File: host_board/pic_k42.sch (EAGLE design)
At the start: 57 parts, among them IC1 PIC18F57K42-E_PT, IC2 REF3440IDBVR, IC3 MAX232, IC4 ILAMP, K1 G6K-2P, Q1 ASF1, X1 RX-2, X2 TX-2, X3 RESETJMP, X4 MINI-USB-UX60A-MB-5ST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

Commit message: mbmc version
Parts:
- added R12: 220, rcl:R-US_R1206
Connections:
- new net N$70: C1.1, R12.1, R2.1, S4.4, X3-2.S
- net N$1: now also R12.2; no longer C1.1, R2.1, S4.4, X3-2.S
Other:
- moved on the sheet: C1, R2
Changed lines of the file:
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@@
 <?xml version="1.0" encoding="utf-8"?>
 <!DOCTYPE eagle SYSTEM "eagle.dtd">
-<eagle version="9.5.0">
+<eagle version="9.5.1">
 <drawing>
 <settings>
@@
 <part name="TP2" library="testpad" library_urn="urn:adsk.eagle:library:385" deviceset="TP" device="B1,27" package3d_urn="urn:adsk.eagle:package:27944/2"/>
 <part name="VDD10" library="supply1" library_urn="urn:adsk.eagle:library:371" deviceset="VDD" device=""/>
+<part name="R12" library="rcl" library_urn="urn:adsk.eagle:library:334" deviceset="R-US_" device="R1206" package3d_urn="urn:adsk.eagle:package:23540/2" value="220"/>
 </parts>
 <sheets>
@@
 <attribute name="VALUE" x="61.722" y="1.27" size="1.778" layer="96" rot="R90"/>
 </instance>
-<instance part="R2" gate="G$1" x="53.34" y="0" smashed="yes" rot="R180">
-<attribute name="NAME" x="57.15" y="-1.4986" size="1.778" layer="95" rot="R180"/>
-<attribute name="VALUE" x="57.15" y="3.302" size="1.778" layer="96" rot="R180"/>
-</instance>
-<instance part="C1" gate="G$1" x="58.42" y="-2.54" smashed="yes">
-<attribute name="NAME" x="59.436" y="-1.905" size="1.778" layer="95"/>
-<attribute name="VALUE" x="59.436" y="-6.731" size="1.778" layer="96"/>
-</instance>
-<instance part="VDD1" gate="G$1" x="45.72" y="0" smashed="yes" rot="R90">
-<attribute name="VALUE" x="48.26" y="-2.54" size="1.778" layer="96" rot="R180"/>
-</instance>
-<instance part="VSS1" gate="G$1" x="58.42" y="-10.16" smashed="yes">
-<attribute name="VALUE" x="55.88" y="-15.24" size="1.778" layer="96" rot="R90"/>
+<instance part="R2" gate="G$1" x="53.34" y="-10.16" smashed="yes" rot="R180">
+<attribute name="NAME" x="57.15" y="-11.6586" size="1.778" layer="95" rot="R180"/>
+<attribute name="VALUE" x="57.15" y="-6.858" size="1.778" layer="96" rot="R180"/>
+</instance>
+<instance part="C1" gate="G$1" x="58.42" y="-12.7" smashed="yes">
+<attribute name="NAME" x="59.436" y="-12.065" size="1.778" layer="95"/>
+<attribute name="VALUE" x="59.436" y="-16.891" size="1.778" layer="96"/>
+</instance>
+<instance part="VDD1" gate="G$1" x="48.26" y="2.54" smashed="yes">
+<attribute name="VALUE" x="45.72" y="0" size="1.778" layer="96" rot="R90"/>
+</instance>
+<instance part="VSS1" gate="G$1" x="50.8" y="-20.32" smashed="yes">
+<attribute name="VALUE" x="48.26" y="-25.4" size="1.778" layer="96" rot="R90"/>
 </instance>
 <instance part="VDD2" gate="G$1" x="58.42" y="-22.86" smashed="yes" rot="R90">
@@
 <instance part="VDD10" gate="G$1" x="-106.68" y="-48.26" smashed="yes" rot="R180">
 <attribute name="VALUE" x="-104.14" y="-45.72" size="1.778" layer="96" rot="R270"/>
+</instance>
+<instance part="R12" gate="G$1" x="58.42" y="-5.08" smashed="yes" rot="R90">
+<attribute name="NAME" x="56.9214" y="-8.89" size="1.778" layer="95" rot="R90"/>
+<attribute name="VALUE" x="61.722" y="-8.89" size="1.778" layer="96" rot="R90"/>
 </instance>
 </instances>
@@
 </busses>
 <nets>
-<net name="N$1" class="0">
-<segment>
-<pinref part="R1" gate="G$1" pin="1"/>
-<pinref part="R2" gate="G$1" pin="1"/>
-<pinref part="C1" gate="G$1" pin="1"/>
-<junction x="58.42" y="0"/>
-<pinref part="SV1" gate="1" pin="1"/>
-<wire x1="63.5" y1="-50.8" x2="63.5" y2="-17.78" width="0.1524" layer="91"/>
-<wire x1="63.5" y1="-17.78" x2="63.5" y2="0" width="0.1524" layer="91"/>
-<wire x1="63.5" y1="0" x2="58.42" y2="0" width="0.1524" layer="91"/>
-<junction x="63.5" y="-50.8"/>
-<wire x1="63.5" y1="0" x2="73.66" y2="0" width="0.1524" layer="91"/>
-<pinref part="X3" gate="-2" pin="S"/>
-<wire x1="73.66" y1="0" x2="73.66" y2="7.62" width="0.1524" layer="91"/>
-<junction x="63.5" y="0"/>
-<junction x="73.66" y="7.62"/>
-<wire x1="63.5" y1="-17.78" x2="139.7" y2="-17.78" width="0.1524" layer="91"/>
-<junction x="63.5" y="-17.78"/>
-<wire x1="139.7" y1="-17.78" x2="139.7" y2="-35.56" width="0.1524" layer="91"/>
-<wire x1="139.7" y1="-35.56" x2="167.64" y2="-35.56" width="0.1524" layer="91"/>
-<pinref part="S4" gate="G$1" pin="4"/>
-<wire x1="167.64" y1="-35.56" x2="167.64" y2="-43.18" width="0.1524" layer="91"/>
-<junction x="167.64" y="-43.18"/>
-</segment>
-</net>
 <net name="N$2" class="0">
 <segment>
@@
 <wire x1="58.42" y1="17.78" x2="58.42" y2="10.16" width="0.1524" layer="91"/>
 <junction x="58.42" y="17.78"/>
+<junction x="58.42" y="10.16"/>
 </segment>
 </net>
@@
 <pinref part="R2" gate="G$1" pin="2"/>
 <pinref part="VDD1" gate="G$1" pin="VDD"/>
-<junction x="48.26" y="0"/>
+<wire x1="48.26" y1="-10.16" x2="48.26" y2="0" width="0.1524" layer="91"/>
+<junction x="48.26" y="-10.16"/>
 </segment>
 <segment>
@@
 <pinref part="VDD2" gate="G$1" pin="VDD"/>
 <junction x="60.96" y="-50.8"/>
+<junction x="60.96" y="-22.86"/>
 </segment>
 <segment>
@@
 <pinref part="VSS2" gate="G$1" pin="VSS"/>
 <junction x="58.42" y="-50.8"/>
+<junction x="58.42" y="-30.48"/>
 </segment>
 <segment>
@@
 <pinref part="C1" gate="G$1" pin="2"/>
 <pinref part="VSS1" gate="G$1" pin="VSS"/>
-<junction x="58.42" y="-7.62"/>
+<wire x1="50.8" y1="-17.78" x2="58.42" y2="-17.78" width="0.1524" layer="91"/>
+<junction x="58.42" y="-17.78"/>
+<junction x="50.8" y="-17.78"/>
 </segment>
 <segment>
@@
 </segment>
 </net>
+<net name="N$70" class="0">
+<segment>
+<pinref part="C1" gate="G$1" pin="1"/>
+<pinref part="R2" gate="G$1" pin="1"/>
+<pinref part="R12" gate="G$1" pin="1"/>
+<pinref part="R12" gate="G$1" pin="1"/>
+<junction x="58.42" y="-10.16"/>
+<junction x="58.42" y="-10.16"/>
+<wire x1="58.42" y1="-10.16" x2="66.04" y2="-10.16" width="0.1524" layer="91"/>
+<wire x1="66.04" y1="-10.16" x2="66.04" y2="-25.4" width="0.1524" layer="91"/>
+<wire x1="66.04" y1="-25.4" x2="76.2" y2="-25.4" width="0.1524" layer="91"/>
+<pinref part="X3" gate="-2" pin="S"/>
+<junction x="73.66" y="7.62"/>
+<wire x1="73.66" y1="-2.54" x2="73.66" y2="7.62" width="0.1524" layer="91"/>
+<wire x1="73.66" y1="-2.54" x2="76.2" y2="-2.54" width="0.1524" layer="91"/>
+<wire x1="76.2" y1="-17.78" x2="139.7" y2="-17.78" width="0.1524" layer="91"/>
+<wire x1="139.7" y1="-17.78" x2="139.7" y2="-35.56" width="0.1524" layer="91"/>
+<wire x1="139.7" y1="-35.56" x2="167.64" y2="-35.56" width="0.1524" layer="91"/>
+<pinref part="S4" gate="G$1" pin="4"/>
+<wire x1="167.64" y1="-35.56" x2="167.64" y2="-43.18" width="0.1524" layer="91"/>
+<junction x="167.64" y="-43.18"/>
+<wire x1="76.2" y1="-2.54" x2="76.2" y2="-17.78" width="0.1524" layer="91"/>
+<wire x1="76.2" y1="-25.4" x2="76.2" y2="-17.78" width="0.1524" layer="91"/>
+<junction x="76.2" y="-17.78"/>
+</segment>
+</net>
+<net name="N$1" class="0">
+<segment>
+<pinref part="R1" gate="G$1" pin="1"/>
+<pinref part="R12" gate="G$1" pin="2"/>
+<junction x="58.42" y="0"/>
+<wire x1="58.42" y1="0" x2="63.5" y2="0" width="0.1524" layer="91"/>
+<pinref part="SV1" gate="1" pin="1"/>
+<wire x1="63.5" y1="-50.8" x2="63.5" y2="0" width="0.1524" layer="91"/>
+<junction x="63.5" y="-50.8"/>
+</segment>
+</net>

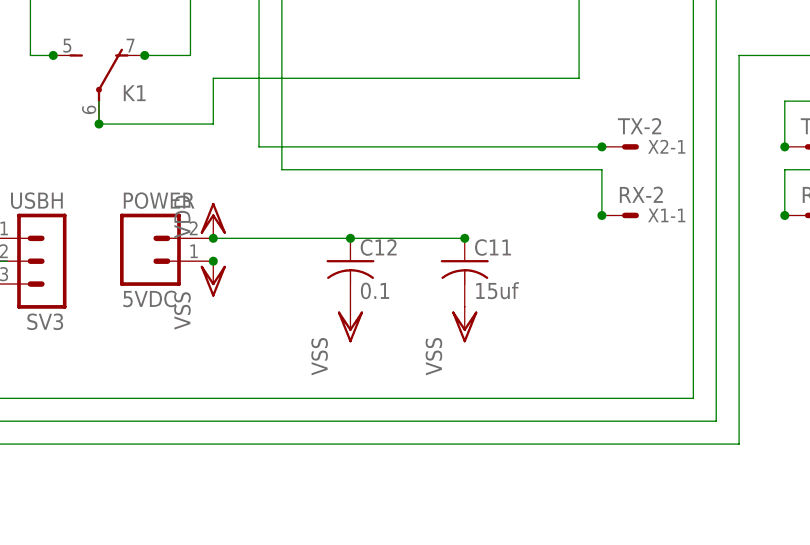
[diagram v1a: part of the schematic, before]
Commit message: up host board to v1.7
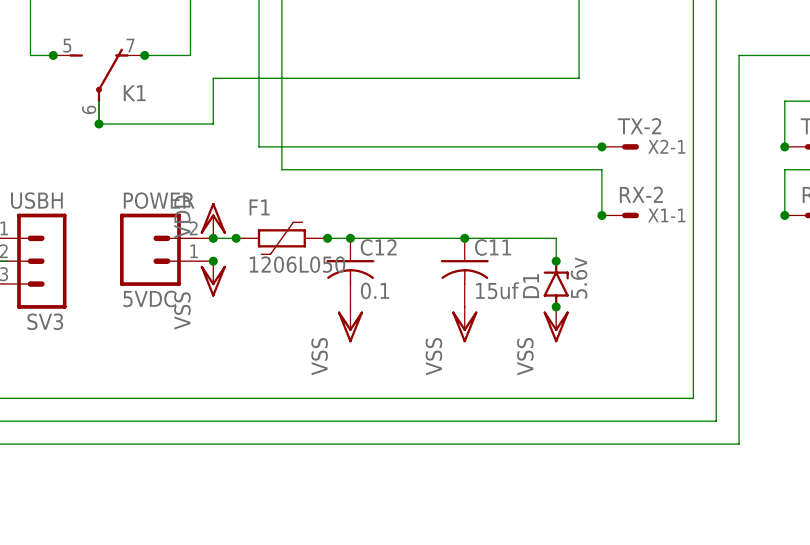
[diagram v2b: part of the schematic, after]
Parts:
- added D1: 5.6v, diode:ZENER-DIODEDO34-7
- added F1: 1206L050, polyfuse-smd_10:1206L050
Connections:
- new net N$71: C11.1, C12.1, D1.C, F1.1
- net VDD: now also F1.2; no longer C11.1, C12.1
- net VSS: now also D1.A
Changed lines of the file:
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@@
 <layer number="97" name="Info" color="7" fill="1" visible="yes" active="yes"/>
 <layer number="98" name="Guide" color="6" fill="1" visible="yes" active="yes"/>
+<layer number="99" name="SpiceOrder" color="5" fill="1" visible="yes" active="yes"/>
 </layers>
 <schematic xreflabel="%F%N/%S.%C%R" xrefpart="/%S.%C%R">
@@
 <classes>
 <class number="0" name="default" width="0" drill="0">
+</class>
+<class number="1" name="i-line" width="0.3" drill="0">
 </class>
 </classes>
@@
 <part name="VDD10" library="supply1" library_urn="urn:adsk.eagle:library:371" deviceset="VDD" device=""/>
 <part name="R12" library="rcl" library_urn="urn:adsk.eagle:library:334" deviceset="R-US_" device="R1206" package3d_urn="urn:adsk.eagle:package:23540/2" value="220"/>
+<part name="VSS16" library="supply1" library_urn="urn:adsk.eagle:library:371" deviceset="VSS" device=""/>
+<part name="F1" library="polyfuse-smd_10" deviceset="?" device="1206L" technology="050"/>
+<part name="D1" library="diode" library_urn="urn:adsk.eagle:library:210" deviceset="ZENER-DIODE" device="DO34-7" package3d_urn="urn:adsk.eagle:package:43364/1" value="5.6v"/>
 </parts>
 <sheets>
@@
 <attribute name="VALUE" x="61.722" y="-8.89" size="1.778" layer="96" rot="R90"/>
 </instance>
+<instance part="VSS16" gate="G$1" x="-7.62" y="-50.8" smashed="yes">
+<attribute name="VALUE" x="-10.16" y="-55.88" size="1.778" layer="96" rot="R90"/>
+</instance>
+<instance part="F1" gate="G$1" x="-38.1" y="-40.64" smashed="yes">
+<attribute name="NAME" x="-41.91" y="-38.1" size="1.778" layer="95"/>
+<attribute name="VALUE" x="-41.91" y="-44.45" size="1.778" layer="96"/>
+</instance>
+<instance part="D1" gate="G$1" x="-7.62" y="-45.72" smashed="yes" rot="R90">
+<attribute name="NAME" x="-9.525" y="-47.498" size="1.778" layer="95" rot="R90"/>
+<attribute name="VALUE" x="-4.191" y="-47.498" size="1.778" layer="96" rot="R90"/>
+</instance>
 </instances>
 <busses>
@@
 </segment>
 </net>
-<net name="VDD" class="0">
+<net name="VDD" class="1">
 <segment>
 <pinref part="R2" gate="G$1" pin="2"/>
@@
 <pinref part="POWER" gate="G$1" pin="2"/>
 <pinref part="VDD13" gate="G$1" pin="VDD"/>
+<pinref part="F1" gate="G$1" pin="2"/>
+<wire x1="-45.72" y1="-40.64" x2="-43.18" y2="-40.64" width="0.1524" layer="91"/>
+<junction x="-43.18" y="-40.64"/>
 <junction x="-45.72" y="-40.64"/>
-<wire x1="-45.72" y1="-40.64" x2="-30.48" y2="-40.64" width="0.3048" layer="91"/>
-<pinref part="C11" gate="G$1" pin="1"/>
-<pinref part="C12" gate="G$1" pin="1"/>
-<wire x1="-30.48" y1="-40.64" x2="-17.78" y2="-40.64" width="0.3048" layer="91"/>
-<junction x="-30.48" y="-40.64"/>
-<junction x="-17.78" y="-40.64"/>
 </segment>
 <segment>
@@
 </segment>
 </net>
-<net name="VSS" class="0">
+<net name="VSS" class="1">
 <segment>
 <pinref part="SV1" gate="1" pin="3"/>
@@
 <pinref part="VSS15" gate="G$1" pin="VSS"/>
 <wire x1="-111.76" y1="-43.18" x2="-111.76" y2="-45.72" width="0.1524" layer="91"/>
+</segment>
+<segment>
+<pinref part="VSS16" gate="G$1" pin="VSS"/>
+<pinref part="D1" gate="G$1" pin="A"/>
+<junction x="-7.62" y="-48.26"/>
 </segment>
 </net>
@@
 <pinref part="R2" gate="G$1" pin="1"/>
 <pinref part="R12" gate="G$1" pin="1"/>
-<pinref part="R12" gate="G$1" pin="1"/>
 <junction x="58.42" y="-10.16"/>
 <junction x="58.42" y="-10.16"/>
@@
 </segment>
 </net>
+<net name="N$71" class="0">
+<segment>
+<pinref part="C11" gate="G$1" pin="1"/>
+<pinref part="C12" gate="G$1" pin="1"/>
+<wire x1="-30.48" y1="-40.64" x2="-17.78" y2="-40.64" width="0.3048" layer="91"/>
+<junction x="-17.78" y="-40.64"/>
+<wire x1="-17.78" y1="-40.64" x2="-7.62" y2="-40.64" width="0.1524" layer="91"/>
+<wire x1="-7.62" y1="-40.64" x2="-7.62" y2="-43.18" width="0.1524" layer="91"/>
+<pinref part="F1" gate="G$1" pin="1"/>
+<wire x1="-30.48" y1="-40.64" x2="-33.02" y2="-40.64" width="0.1524" layer="91"/>
+<junction x="-33.02" y="-40.64"/>
+<junction x="-30.48" y="-40.64"/>
+<pinref part="D1" gate="G$1" pin="C"/>
+<junction x="-7.62" y="-43.18"/>
+</segment>
+</net>
